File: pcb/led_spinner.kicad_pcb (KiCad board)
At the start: 2 copper layers, 48.3 x 48.3 mm, 43 parts, among them CON1 AVR-ISP-6, J1 SERIAL, J2 SPARE, J3 TILT, SW1 SW_PUSH_ALT, U1 ATMEGA48_88_168_328P-32SMD

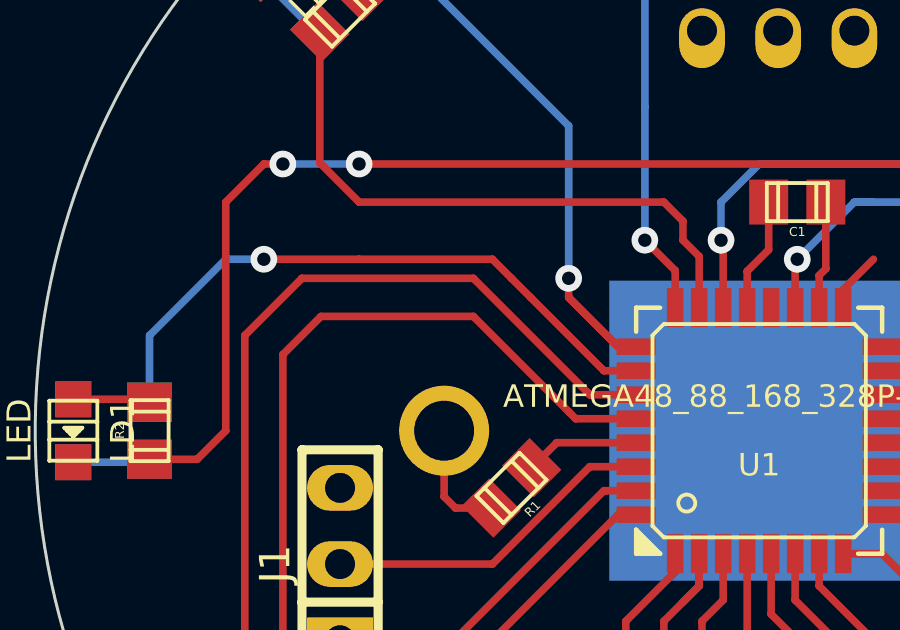
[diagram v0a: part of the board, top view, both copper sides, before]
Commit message: Remove some extra overlapping track segments.
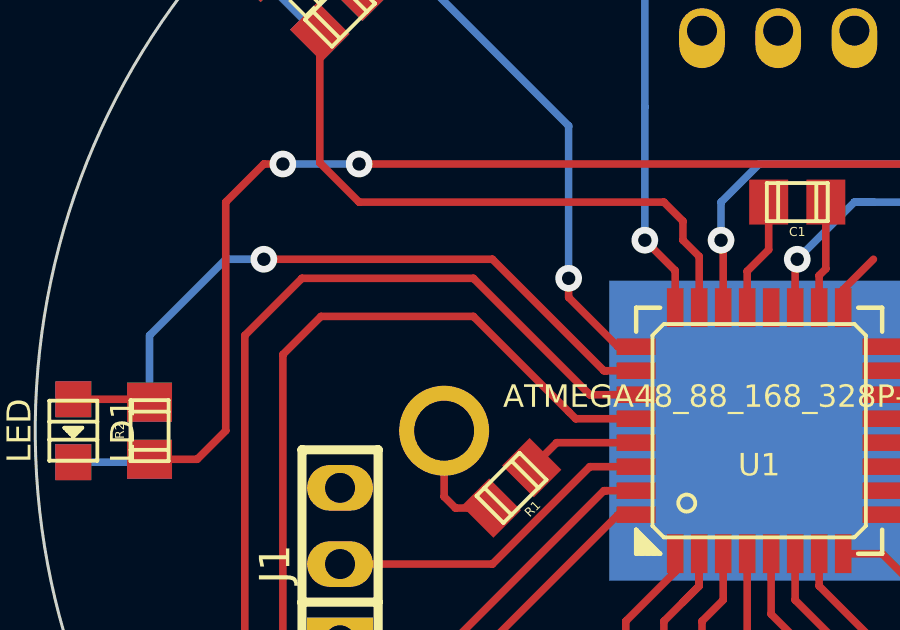
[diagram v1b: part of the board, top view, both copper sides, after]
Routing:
- net /BNE: track 20.3 -> 17.9 mm
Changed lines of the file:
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@@
     (thickness 1.6)
     (drawings 7)
-    (tracks 278)
+    (tracks 275)
     (zones 0)
     (modules 43)
@@
   (segment (start 193.91122 110.77956) (end 193.91122 113.74628) (width 0.254) (layer F.Cu) (net 1))
   (segment (start 193.91122 113.74628) (end 193.675 113.9825) (width 0.254) (layer F.Cu) (net 1))
+  (segment (start 185.42 100.965) (end 177.8 100.965) (width 0.254) (layer F.Cu) (net 2))
+  (segment (start 189.23 104.68102) (end 189.13602 104.68102) (width 0.254) (layer F.Cu) (net 2))
+  (segment (start 190.21044 104.68102) (end 189.23 104.68102) (width 0.254) (layer F.Cu) (net 2))
+  (via (at 177.8 100.965) (size 0.889) (layers F.Cu B.Cu) (net 2))
+  (segment (start 176.53 100.965) (end 173.99 103.505) (width 0.254) (layer B.Cu) (net 2))
+  (segment (start 173.99 103.505) (end 173.99 105.7275) (width 0.254) (layer B.Cu) (net 2))
   (segment (start 177.8 100.965) (end 176.53 100.965) (width 0.254) (layer B.Cu) (net 2))
-  (segment (start 173.99 103.505) (end 173.99 105.7275) (width 0.254) (layer B.Cu) (net 2))
-  (segment (start 176.53 100.965) (end 173.99 103.505) (width 0.254) (layer B.Cu) (net 2))
-  (segment (start 186.69 102.235) (end 186.055 101.6) (width 0.254) (layer F.Cu) (net 2))
-  (segment (start 189.13602 104.68102) (end 186.69 102.235) (width 0.254) (layer F.Cu) (net 2))
-  (segment (start 190.21044 104.68102) (end 189.13602 104.68102) (width 0.254) (layer F.Cu) (net 2))
-  (via (at 177.8 100.965) (size 0.889) (layers F.Cu B.Cu) (net 2))
-  (segment (start 180.975 100.965) (end 177.8 100.965) (width 0.254) (layer F.Cu) (net 2))
-  (segment (start 185.42 100.965) (end 180.975 100.965) (width 0.254) (layer F.Cu) (net 2))
-  (segment (start 186.055 101.6) (end 185.42 100.965) (width 0.254) (layer F.Cu) (net 2))
+  (segment (start 189.13602 104.68102) (end 185.42 100.965) (width 0.254) (layer F.Cu) (net 2))
   (segment (start 190.5 88.9) (end 191.135 88.265) (width 0.254) (layer B.Cu) (net 3))
   (segment (start 195.2625 87.3125) (end 195.2625 86.36) (width 0.254) (layer B.Cu) (net 3))
@@
   (segment (start 182.88 91.44) (end 181.61 91.44) (width 0.254) (layer B.Cu) (net 4))
   (segment (start 190.21044 103.88092) (end 189.60592 103.88092) (width 0.254) (layer F.Cu) (net 4))
-  (segment (start 189.60592 103.88092) (end 187.96 102.235) (width 0.254) (layer F.Cu) (net 4))
   (segment (start 187.96 102.235) (end 187.96 101.6) (width 0.254) (layer F.Cu) (net 4))
   (via (at 187.96 101.6) (size 0.889) (layers F.Cu B.Cu) (net 4))

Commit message: Route ICSP header. Route battery connections.
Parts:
- moved CON1 0.63 mm to (194.3, 92.1), turned to 90 degrees
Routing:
- net +BATT: track 16.6 -> 83.4 mm, vias 0 -> 5
- net /SCK: track 2.03 -> 29.8 mm, vias 0 -> 2
- net /~RESET: track 3.83 -> 31.5 mm, vias 0 -> 2
- net /MISO: track 4.95 -> 27.3 mm, vias 0 -> 2
- net /MOSI: track 6.92 -> 28.6 mm, vias 0 -> 2
- net /BN: track 20.5 -> 23.8 mm
- net /BNE: track 17.9 -> 20.5 mm
- net /BUTTON: track 10.9 -> 13.2 mm
- net /FW: track 45.6 -> 47.4 mm
- net /FN: track 45.7 -> 46.4 mm
- net /BSW: track 41.6 -> 41.0 mm

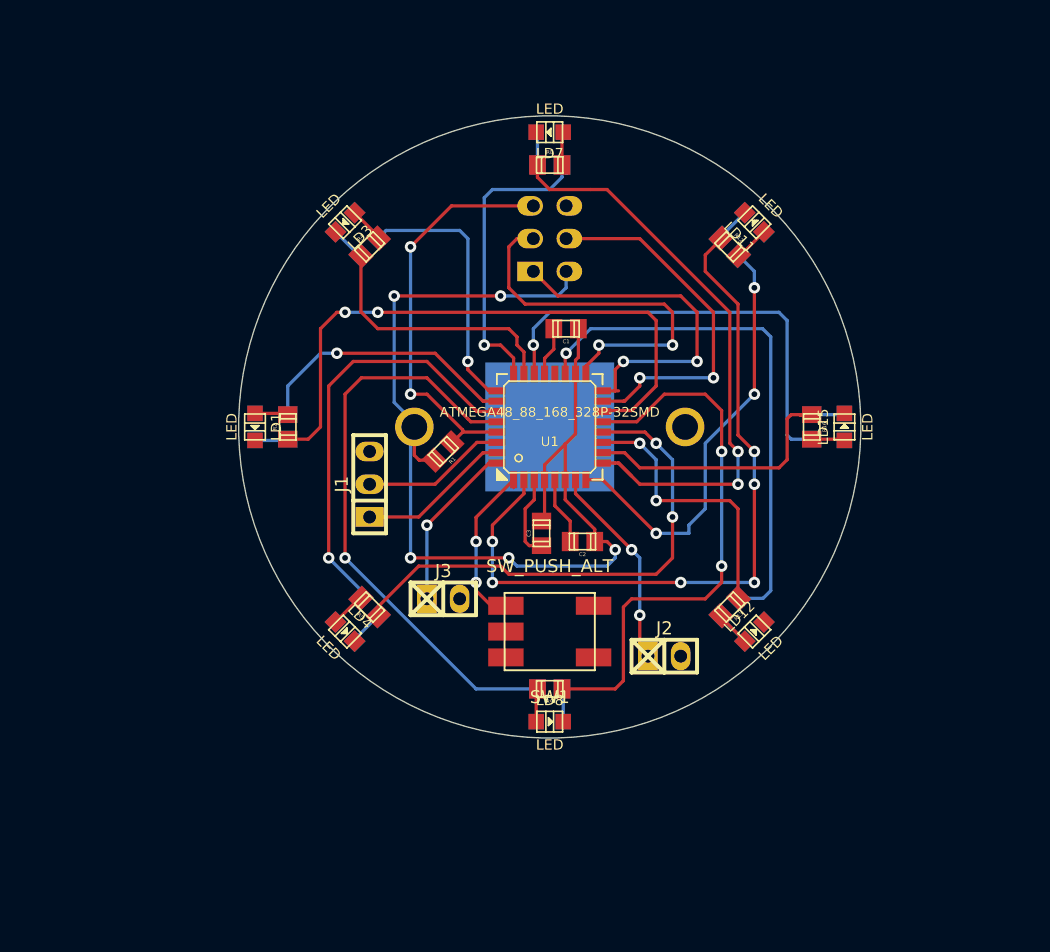
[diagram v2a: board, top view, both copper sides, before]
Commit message: Route ground connections in preparation for ground planes.
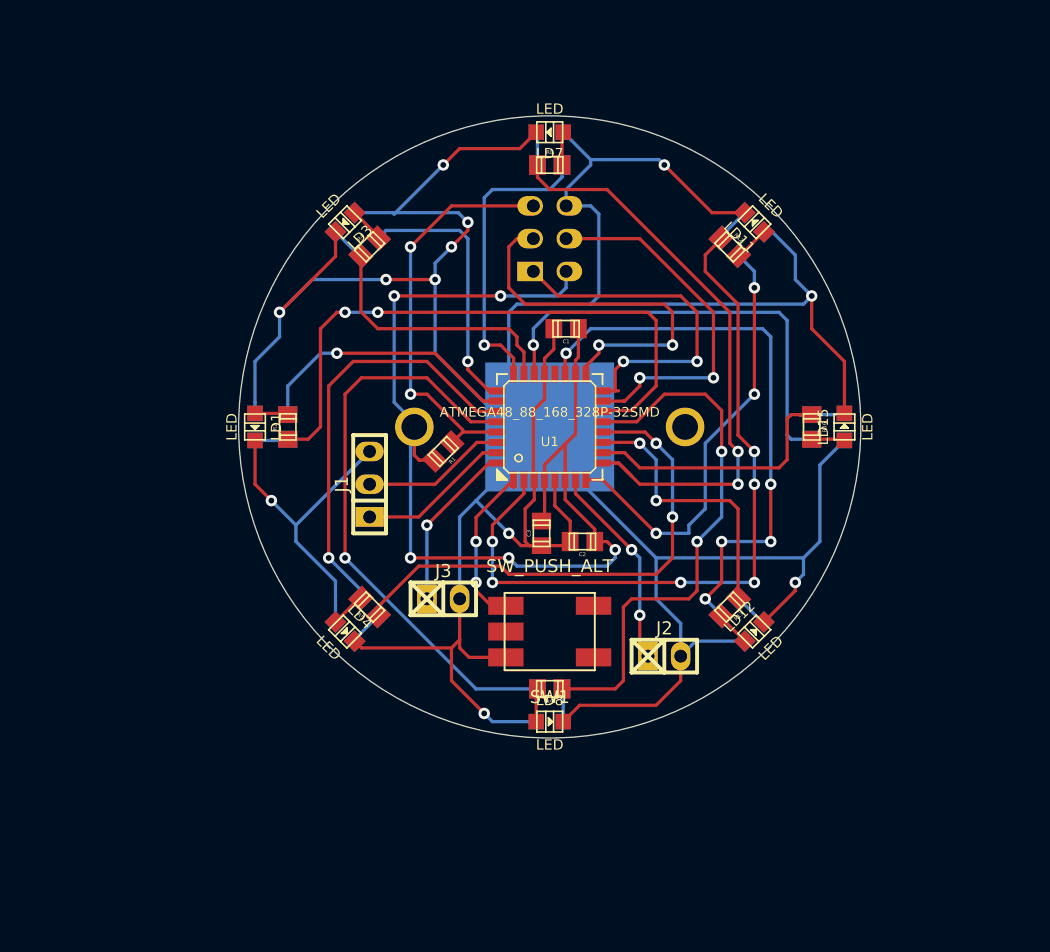
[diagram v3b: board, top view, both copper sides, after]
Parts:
- turned LD6 to 225 degrees
- turned R7 to 45 degrees
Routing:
- net GND: track 15.6 -> 326.1 mm, vias 0 -> 12
- net /BSW: track 41.0 -> 45.0 mm, vias 1 -> 5
- net /FS: track 43.1 -> 42.4 mm

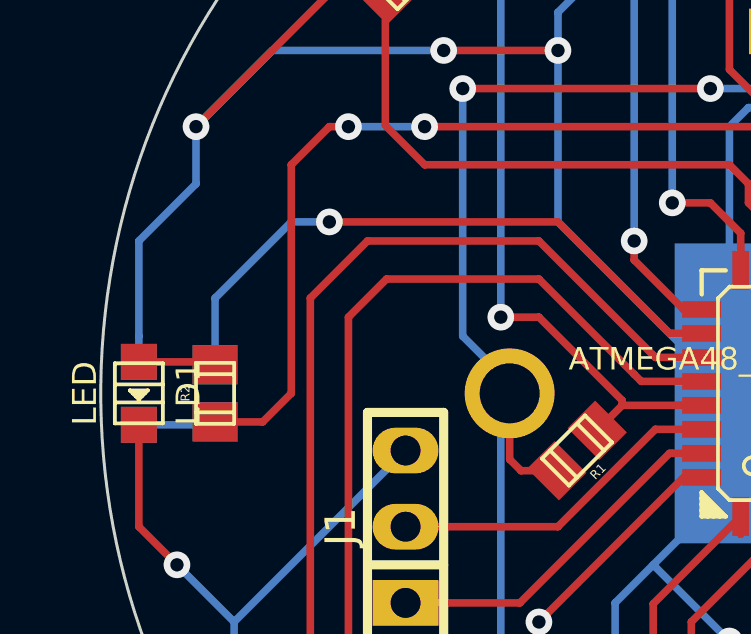
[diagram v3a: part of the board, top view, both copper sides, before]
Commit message: Route one missed ground connection.
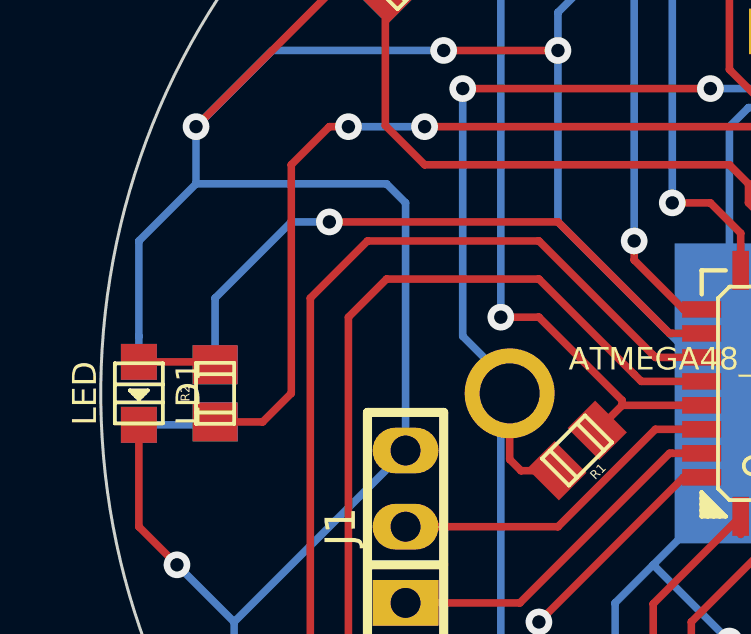
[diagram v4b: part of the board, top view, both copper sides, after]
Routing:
- net GND: track 326.1 -> 341.6 mm
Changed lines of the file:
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@@
   (general
     (links 77)
-    (no_connects 1)
+    (no_connects 0)
     (area 170.129999 82.499999 218.490001 130.860001)
     (thickness 1.6)
     (drawings 7)
-    (tracks 457)
+    (tracks 460)
     (zones 0)
     (modules 43)
@@
   (segment (start 190.21044 107.07878) (end 187.56122 107.07878) (width 0.254) (layer F.Cu) (net 24))
   (segment (start 187.56122 107.07878) (end 186.728519 107.911481) (width 0.254) (layer F.Cu) (net 24))
+  (segment (start 180.34 108.585) (end 180.34 100.33) (width 0.254) (layer B.Cu) (net 25) (status 400000))
+  (segment (start 179.705 99.695) (end 173.355 99.695) (width 0.254) (layer B.Cu) (net 25))
+  (segment (start 180.34 100.33) (end 179.705 99.695) (width 0.254) (layer B.Cu) (net 25))
   (segment (start 213.36 118.745) (end 213.36 119.38) (width 0.254) (layer F.Cu) (net 25))
   (via (at 213.36 118.745) (size 0.889) (layers F.Cu B.Cu) (net 25))
@@
   (segment (start 187.325 85.09) (end 191.99098 85.09) (width 0.254) (layer F.Cu) (net 25))
   (segment (start 171.45 104.775) (end 171.45 101.6) (width 0.254) (layer B.Cu) (net 25))
+  (segment (start 171.45 101.6) (end 173.355 99.695) (width 0.254) (layer B.Cu) (net 25))
   (segment (start 171.45 105.63098) (end 171.45 104.775) (width 0.254) (layer B.Cu) (net 25))
-  (segment (start 171.45 101.6) (end 173.355 99.695) (width 0.254) (layer B.Cu) (net 25))
   (segment (start 173.355 99.695) (end 173.355 97.79) (width 0.254) (layer B.Cu) (net 25))
   (segment (start 177.693231 93.451769) (end 177.693231 91.546769) (width 0.254) (layer F.Cu) (net 25))

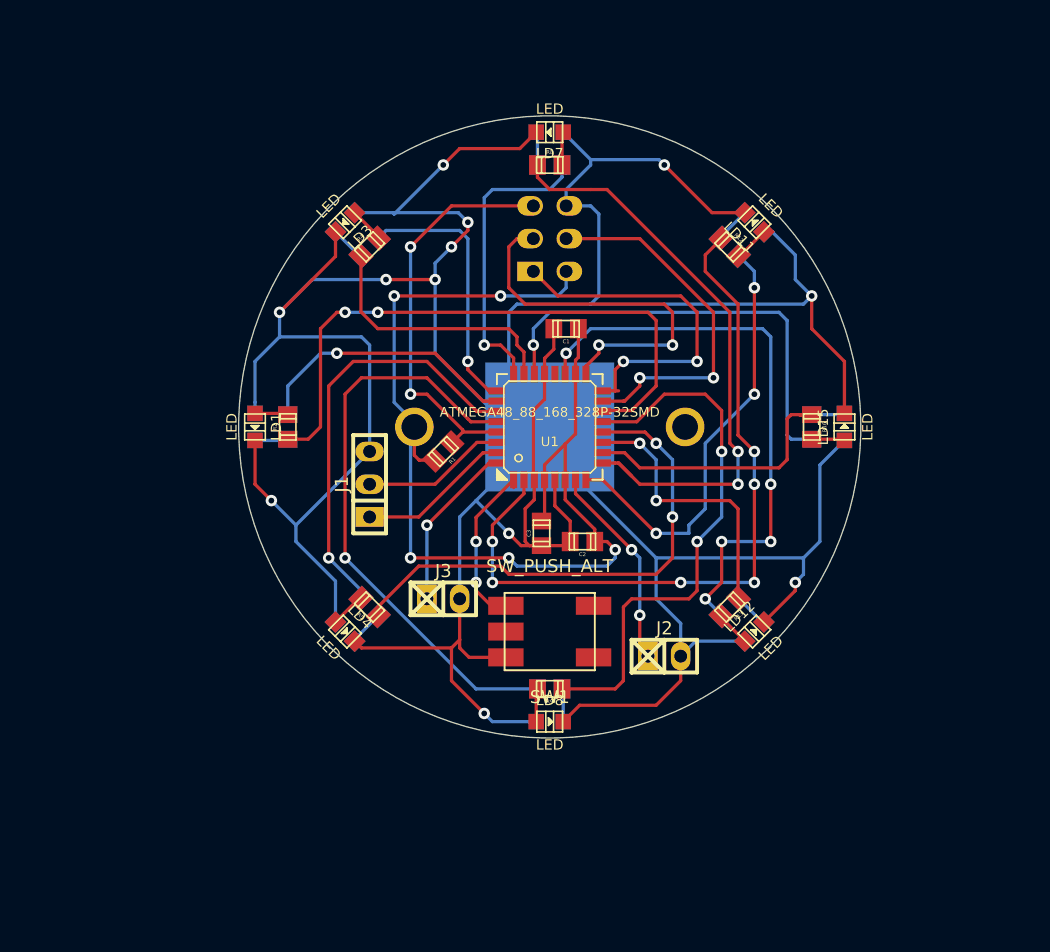
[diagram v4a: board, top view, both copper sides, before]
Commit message: Add ground zone on the front and back.
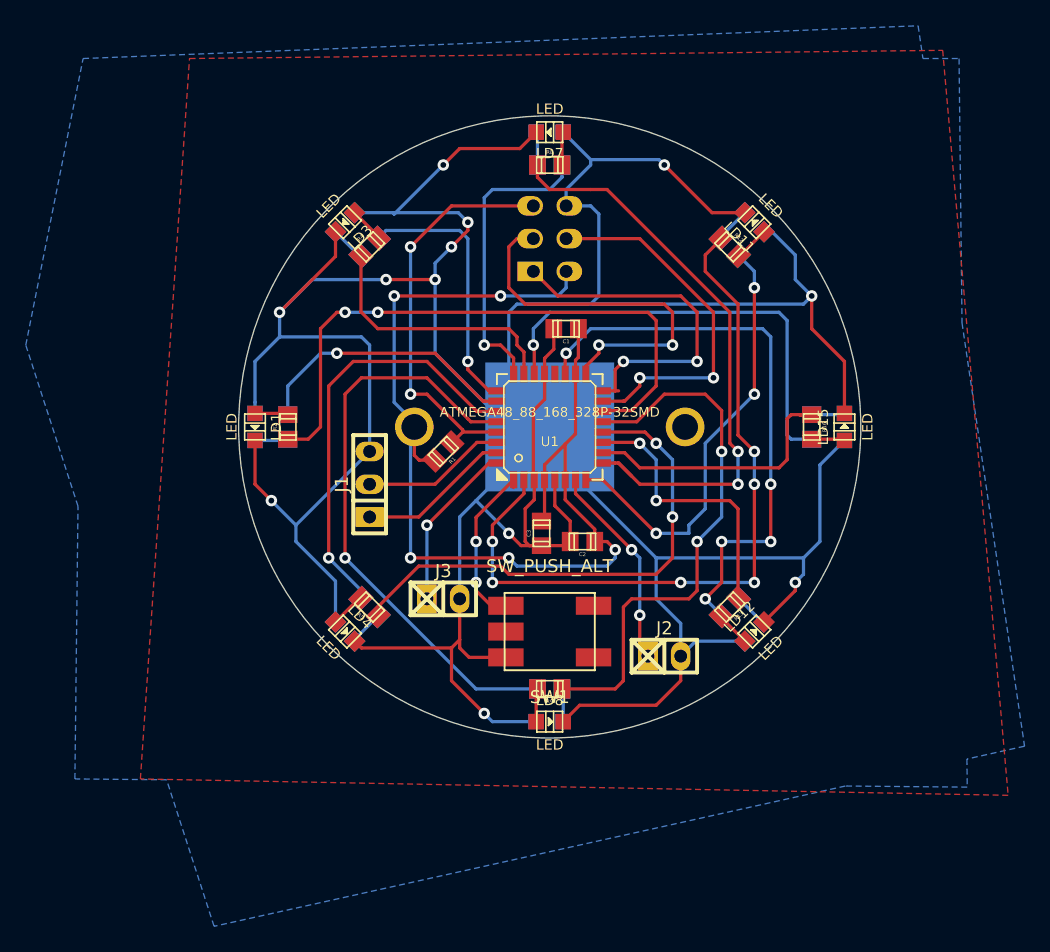
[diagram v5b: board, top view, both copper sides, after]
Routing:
- added copper zone on B.Cu, net GND
- added copper zone on F.Cu, net GND
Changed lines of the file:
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@@
   (segment (start 193.3575 86.36) (end 193.3575 83.91652) (width 0.254) (layer B.Cu) (net 44))
   (segment (start 193.3575 83.91652) (end 193.26098 83.82) (width 0.254) (layer B.Cu) (net 44))
+  (zone (net 25) (net_name GND) (layer B.Cu) (hatch edge 0.508)
+    (connect_pads (clearance 0.508))
+    (min_thickness 0.254)
+    (fill (arc_segments 32) (thermal_gap 0.508) (thermal_bridge_width 0.508))
+    (polygon
+      (pts
+        (xy 231.14 131.445) (xy 226.670485 132.438225) (xy 226.695 134.62) (xy 217.242731 134.533281) (xy 168.275 145.415)
+        (xy 164.593464 134.050261) (xy 157.48 133.985) (xy 157.72036 112.833286) (xy 153.67 100.33) (xy 158.115 78.105)
+        (xy 222.885 75.565) (xy 223.260227 78.105) (xy 226.06 78.105) (xy 226.290477 98.61746) (xy 231.14 131.445)
+      )
+    )
+  )
+  (zone (net 25) (net_name GND) (layer F.Cu) (hatch edge 0.508)
+    (connect_pads (clearance 0.508))
+    (min_thickness 0.254)
+    (fill (arc_segments 32) (thermal_gap 0.508) (thermal_bridge_width 0.508))
+    (polygon
+      (pts
+        (xy 166.37 78.105) (xy 224.79 77.47) (xy 229.87 135.255) (xy 162.56 133.985)
+      )
+    )
+  )
 )
